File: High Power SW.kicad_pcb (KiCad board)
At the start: 2 copper layers, 48 x 48 mm, 20 parts, among them CN1 Jumper_NC_Small, Q1 IRFR7540TRPBF, U1 PS2801C-1-A

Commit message: Fix error's in uploded files
Fix error's in uploded files, for some reason we uploded and old ver.
This has been corrected
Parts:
- removed the ? at (74.6, 109.0)
- BED+, BED-, POWER+, POWER-: footprint MyLib:Keystone_4966 -> MyLib:Keystone_terminal
- moved BED+ 0.90 mm to (96.5, 125.2)
- moved POWER+ 0.90 mm to (85.5, 125.2)
- moved POWER- 0.90 mm to (74.5, 125.2)
- moved BED- 0.75 mm to (107.5, 125.2)

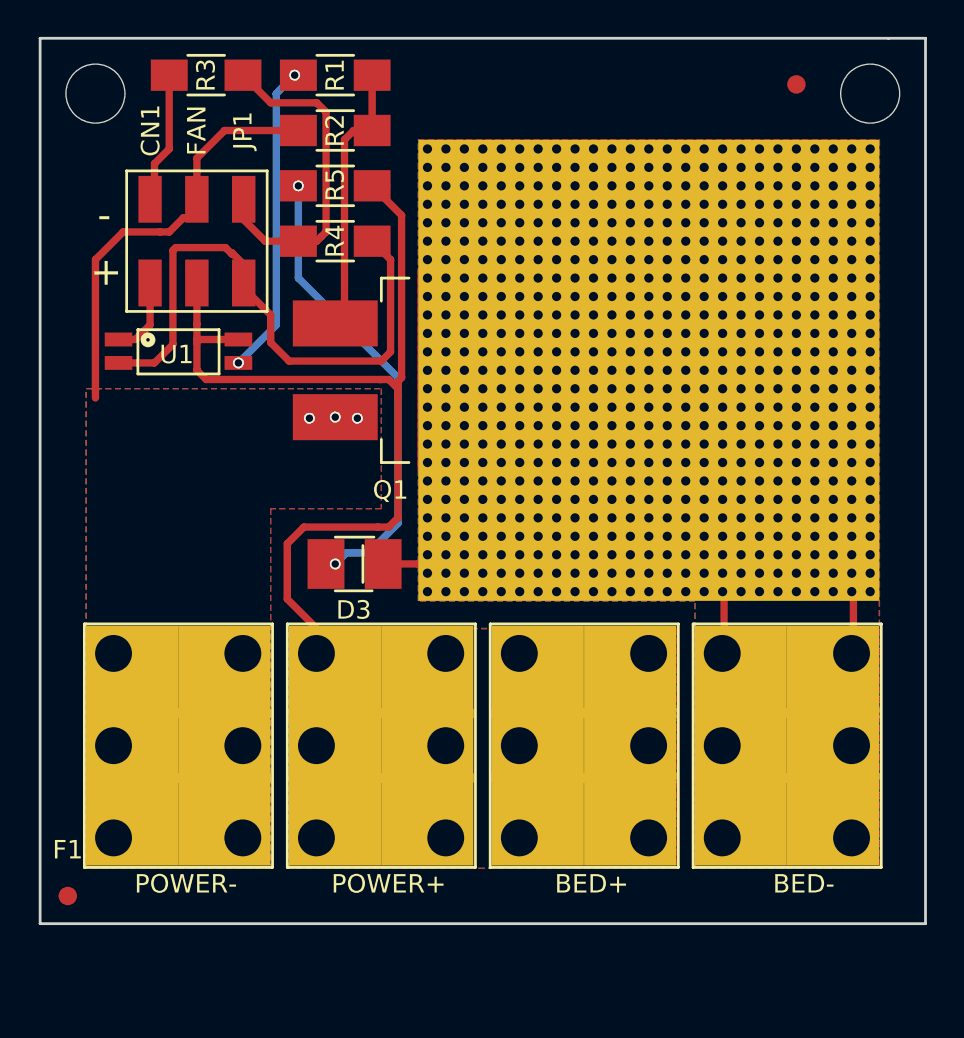
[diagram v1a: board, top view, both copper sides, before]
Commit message: Update Board to have new input opto
Gerber files are not built yet
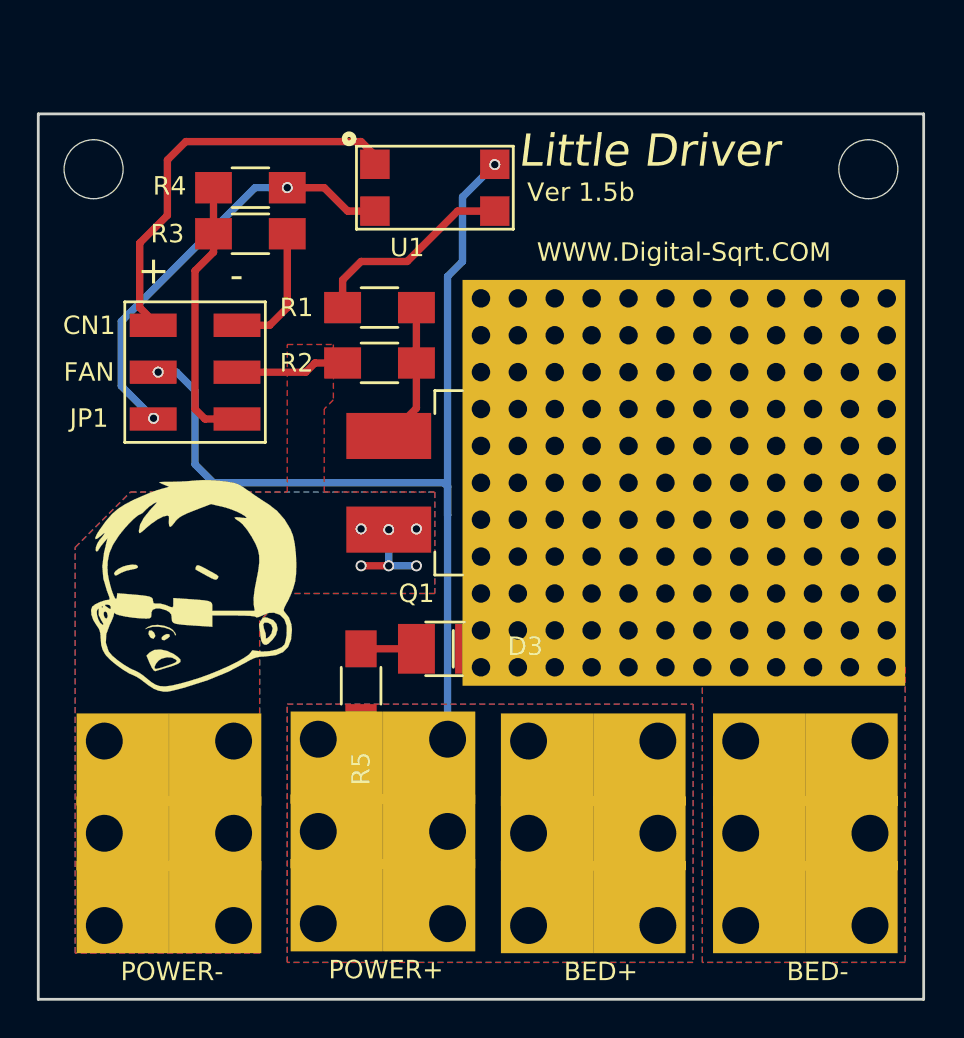
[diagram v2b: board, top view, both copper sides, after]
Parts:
- removed the ? at (79.9, 95.1)
- removed F1 : , Fiducials:Fiducial_1mm_Dia_2.54mm_Outer_CopperTop
- removed F2 : , Fiducials:Fiducial_1mm_Dia_2.54mm_Outer_CopperTop
- added REF***: OSHW-Symbol_6.7x6mm_SilkScreen, Symbols:OSHW-Symbol_6.7x6mm_SilkScreen, B.Cu at (75.0, 116.8)
- ?: moved to F.Cu
- Q1: footprint MyLib:TO-263-2Lead_(Larg_Heat_Sink) -> TO-263-2Lead_(Larg_Heat_Sink_More_Air)
- R5: value 1.8K -> 3.6K
- U1: footprint MyLib:SOP-4 -> MyLib:TLP182
- moved R5 27.1 mm to (84.5, 122.0), turned to 90 degrees
- moved U1 16.5 mm to (88.5, 95.0)
- moved R1 12.8 mm to (85.5, 101.5)
- moved R2 12.8 mm to (85.5, 104.5)
- moved ? 9.59 mm to (75.2, 116.5), turned to 0 degrees
- moved R3 8.93 mm to (78.5, 97.5), turned to 180 degrees
- moved CN1 7.10 mm to (75.5, 105.0), turned to 270 degrees
- moved Q1 6.75 mm to (86.0, 111.0)
- moved D3 6.72 mm to (89.0, 120.0)
- moved R4 5.44 mm to (78.5, 95.0)
- moved BED- 4.85 mm to (108.5, 130.0)
- moved BED+ 4.78 mm to (97.0, 130.0)
- moved POWER- 4.78 mm to (74.0, 130.0)
- moved POWER+ 4.65 mm to (85.6, 129.9)
- moved ? 4.10 mm to (112.0, 94.0)
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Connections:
- CN1 pad 3: (no net) -> +BATT
- CN1 pad 4: (no net) -> GND
- CN1 pad 5: (no net) -> Net-(JP1-Pad1)
- CN1 pad 6: (no net) -> Net-(JP1-Pad2)
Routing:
- net Net-(BED-1-Pad1): track 30.2 -> 0.00 mm
- net Net-(D3-Pad2): track 24.8 -> 3.50 mm, vias 2 -> 0
- net Net-(CN1-Pad1): track 5.31 -> 23.2 mm
- net GND: track 28.0 -> 15.1 mm, vias 3 -> 6
- net Net-(Q1-Pad1): track 15.4 -> 7.58 mm
- net Net-(JP1-Pad1): track 31.5 -> 24.8 mm, vias 0 -> 2
- net Net-(R1-Pad1): track 17.1 -> 11.3 mm, vias 2 -> 0
- net Net-(JP1-Pad2): track 17.4 -> 13.9 mm
- net +BATT: track 52.4 -> 55.1 mm, vias 0 -> 2
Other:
- outline, holes or cut-outs redrawn
- net class Default: clearance 0.2 -> 0.3048
- net class Power: clearance 0.2 -> 0.3048
- net class small_trace: clearance 0.2 -> 0.3048
- rule trace_clearance: 0.2 -> 0.3048
- board text added: "Little Driver"
- board text added: "Ver 1.5b"
- board text added: "WWW.Digital-Sqrt.COM"
- board text removed: "Digital Sqrt"
- board text removed: "Small Driver"
- board text removed: "Ver 1.5"

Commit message: Improve Manufacture cost
Reduced the number of holes,  Moved parts,  Upgraded silk
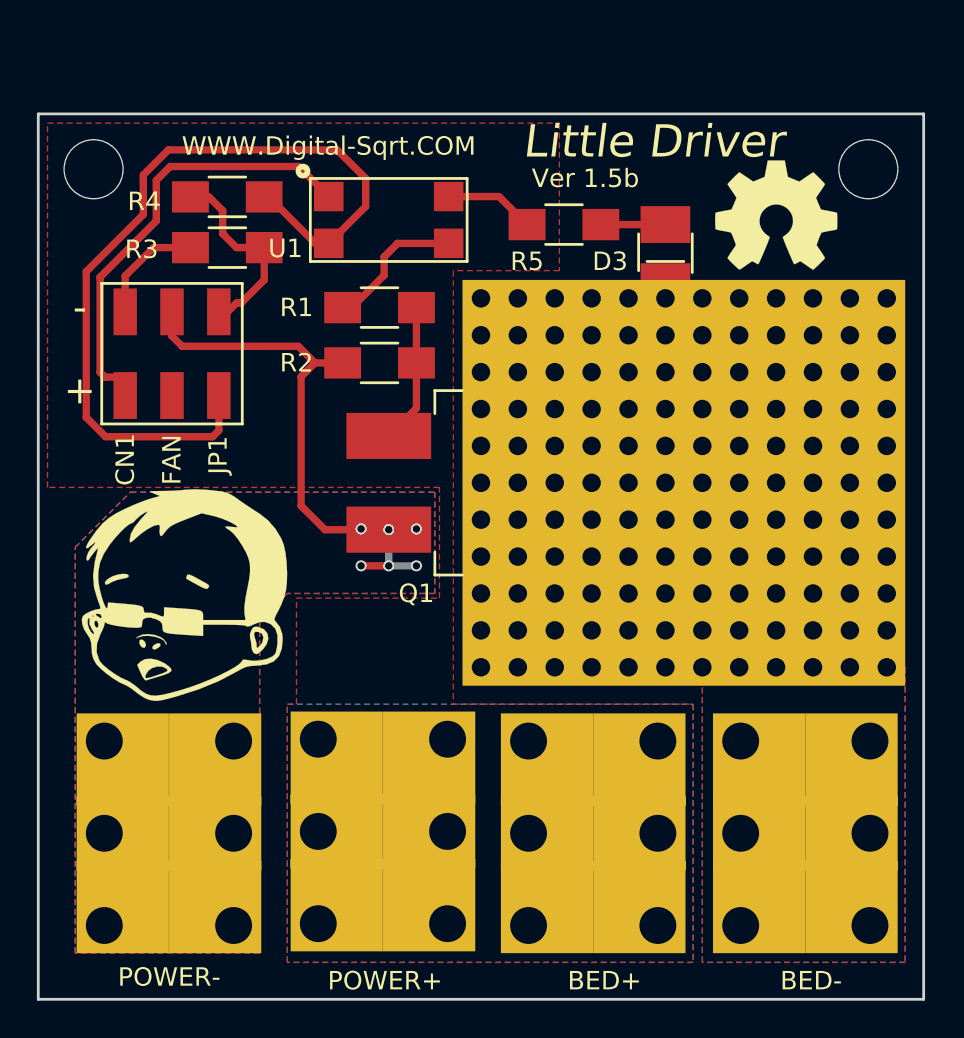
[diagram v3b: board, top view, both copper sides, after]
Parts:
- REF***: moved to F.Cu
- moved REF*** 37.9 mm to (107.0, 96.5), turned to 0 degrees
- moved R5 27.3 mm to (95.5, 97.0), turned to 0 degrees
- moved D3 24.6 mm to (101.0, 98.5), turned to 270 degrees
- moved U1 3.05 mm to (86.0, 96.8)
- moved CN1 1.60 mm to (74.2, 104.0), turned to 0 degrees
- moved R3 1.46 mm to (77.2, 98.2), turned to 0 degrees
- moved R4 1.35 mm to (77.2, 95.5)
- moved ? 0.71 mm to (74.8, 117.0)
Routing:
- net +BATT: track 55.1 -> 4.88 mm, vias 2 -> 0
- net Net-(JP1-Pad1): track 24.8 -> 47.2 mm, vias 2 -> 0
- net GND: track 15.1 -> 32.4 mm
- net Net-(R1-Pad1): track 11.3 -> 7.78 mm
- net Net-(JP1-Pad2): track 13.9 -> 11.5 mm
- net Net-(BED-1-Pad1): track 0.00 -> 1.40 mm
- net Net-(CN1-Pad2): track 8.13 -> 7.12 mm
